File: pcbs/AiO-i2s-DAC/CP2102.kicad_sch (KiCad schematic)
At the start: 12 parts, among them U3 CP2102N

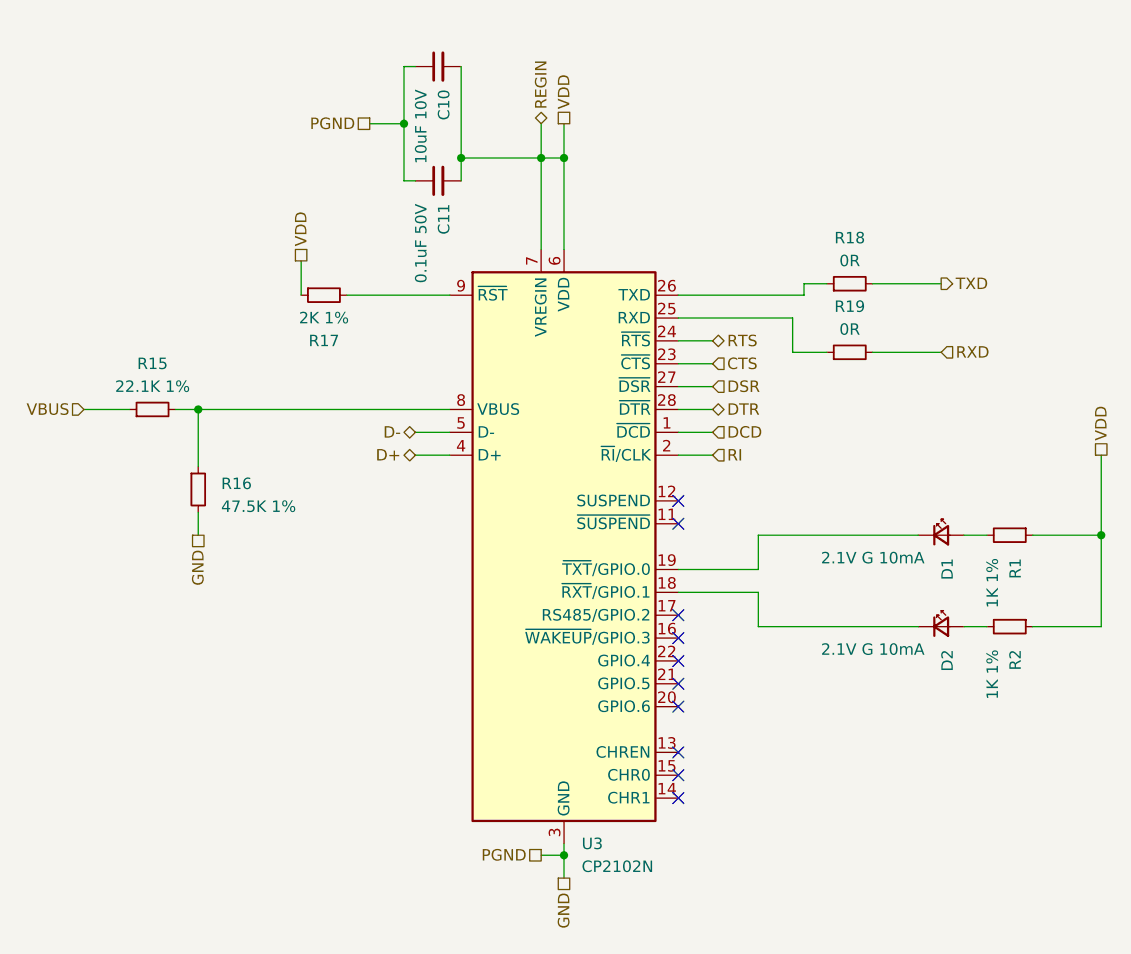
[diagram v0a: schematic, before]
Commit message: Adding equivalent JLCPCB values
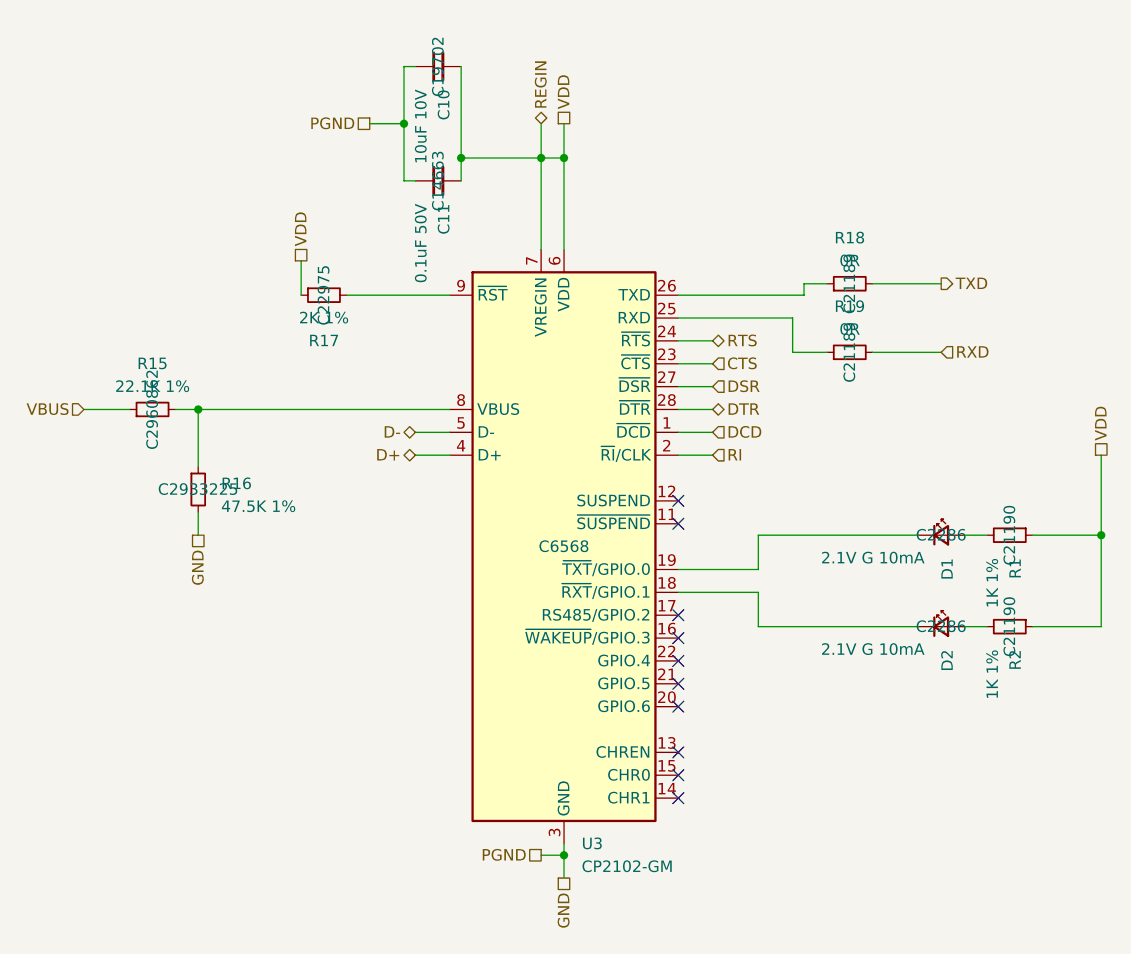
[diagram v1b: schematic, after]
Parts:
- C10: LCSC (none) -> C19702
- C11: LCSC (none) -> C14663
- D1, D2: LCSC (none) -> C2286
- R1, R2: LCSC (none) -> C21190
- R15: LCSC (none) -> C2960862
- R16: LCSC (none) -> C2933225
- R17: LCSC (none) -> C22975
- R18, R19: LCSC (none) -> C21189
- U3: value CP2102N -> CP2102-GM; LCSC (none) -> C6568; Manufacturer_Part_Number CP2102N-A02-GQFN28R -> CP2102-GM
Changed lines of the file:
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@@
+			)
+		)
+		(property "LCSC" "C21190"
+			(at 203.2 100.33 0)
+			(effects
+				(font
+					(size 1.27 1.27)
+				)
 			)
 		)
@@
 			)
 		)
+		(property "LCSC" "C14663"
+			(at 139.7 60.96 0)
+			(effects
+				(font
+					(size 1.27 1.27)
+				)
+			)
+		)
 		(pin "1"
 		)
@@
 			)
 		)
+		(property "LCSC" "C2286"
+			(at 195.58 110.49 0)
+			(effects
+				(font
+					(size 1.27 1.27)
+				)
+			)
+		)
 		(pin "1"
 		)
@@
 				)
 				(hide yes)
+			)
+		)
+		(property "LCSC" "C2286"
+			(at 195.58 100.33 0)
+			(effects
+				(font
+					(size 1.27 1.27)
+				)
 			)
 		)
@@
 			)
 		)
+		(property "LCSC" "C21189"
+			(at 185.42 80.01 0)
+			(effects
+				(font
+					(size 1.27 1.27)
+				)
+			)
+		)
 		(pin "1"
 		)
@@
 			)
 		)
+		(property "LCSC" "C19702"
+			(at 139.7 48.26 0)
+			(effects
+				(font
+					(size 1.27 1.27)
+				)
+			)
+		)
 		(pin "1"
 		)
@@
 			)
 		)
+		(property "LCSC" "C2960862"
+			(at 107.95 86.36 0)
+			(effects
+				(font
+					(size 1.27 1.27)
+				)
+			)
+		)
 		(pin "1"
 		)
@@
 			)
 		)
+		(property "LCSC" "C21190"
+			(at 203.2 110.49 0)
+			(effects
+				(font
+					(size 1.27 1.27)
+				)
+			)
+		)
 		(pin "1"
 		)
@@
 			)
 		)
+		(property "LCSC" "C21189"
+			(at 185.42 72.39 0)
+			(effects
+				(font
+					(size 1.27 1.27)
+				)
+			)
+		)
 		(pin "1"
 		)
@@
 			)
 		)
+		(property "LCSC" "C22975"
+			(at 127 73.66 0)
+			(effects
+				(font
+					(size 1.27 1.27)
+				)
+			)
+		)
 		(pin "1"
 		)
@@
 			)
 		)
+		(property "LCSC" "C2933225"
+			(at 113.03 95.25 0)
+			(effects
+				(font
+					(size 1.27 1.27)
+				)
+			)
+		)
 		(pin "1"
 		)
@@
 			)
 		)
-		(property "Value" "CP2102N"
+		(property "Value" "CP2102-GM"
 			(at 155.6259 137.16 0)
 			(effects
@@
 			)
 		)
-		(property "Datasheet" "https://www.silabs.com/documents/public/data-sheets/cp2102n-datasheet.pdf"
+		(property "Datasheet" "https://www.silabs.com/documents/public/data-sheets/CP2102-9.pdf"
 			(at 154.94 120.65 0)
 			(effects
@@
 			)
 		)
-		(property "Manufacturer_Part_Number" "CP2102N-A02-GQFN28R"
+		(property "Manufacturer_Part_Number" "CP2102-GM"
 			(at 153.67 101.6 0)
 			(effects
@@
 			)
 		)
+		(property "LCSC" "C6568"
+			(at 153.67 101.6 0)
+			(effects
+				(font
+					(size 1.27 1.27)
+				)
+			)
+		)

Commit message: LCSC BOM Preparation
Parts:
- C10: LCSC alt (none) -> C6119842
- C11: LCSC alt (none) -> C1591
- D1, D2: LCSC alt (none) -> C125093
- R1, R2: LCSC alt (none) -> C22548
- R15: LCSC alt (none) -> C2960862
- R16: LCSC alt (none) -> C2933225
- R17: LCSC alt (none) -> C237750
- R18, R19: LCSC alt (none) -> C21189
- U3: LCSC alt (none) -> C6568
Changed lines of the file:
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@@
+			)
+		)
+		(property "LCSC alt" "C22548"
+			(at 203.2 100.33 0)
+			(effects
+				(font
+					(size 1.27 1.27)
+				)
 			)
 		)
@@
 			)
 		)
+		(property "LCSC alt" "C1591"
+			(at 139.7 60.96 0)
+			(effects
+				(font
+					(size 1.27 1.27)
+				)
+			)
+		)
 		(pin "1"
 		)
@@
 			)
 		)
+		(property "LCSC alt" "C125093"
+			(at 195.58 110.49 0)
+			(effects
+				(font
+					(size 1.27 1.27)
+				)
+			)
+		)
 		(pin "1"
 		)
@@
 		)
 		(property "LCSC" "C2286"
+			(at 195.58 100.33 0)
+			(effects
+				(font
+					(size 1.27 1.27)
+				)
+			)
+		)
+		(property "LCSC alt" "C125093"
 			(at 195.58 100.33 0)
 			(effects
@@
 			)
 		)
+		(property "LCSC alt" "C21189"
+			(at 185.42 80.01 0)
+			(effects
+				(font
+					(size 1.27 1.27)
+				)
+			)
+		)
 		(pin "1"
 		)
@@
 			)
 		)
+		(property "LCSC alt" "C6119842"
+			(at 139.7 48.26 0)
+			(effects
+				(font
+					(size 1.27 1.27)
+				)
+			)
+		)
 		(pin "1"
 		)
@@
 			)
 		)
+		(property "LCSC alt" "C2960862"
+			(at 107.95 86.36 0)
+			(effects
+				(font
+					(size 1.27 1.27)
+				)
+			)
+		)
 		(pin "1"
 		)
@@
 			)
 		)
+		(property "LCSC alt" "C22548"
+			(at 203.2 110.49 0)
+			(effects
+				(font
+					(size 1.27 1.27)
+				)
+			)
+		)
 		(pin "1"
 		)
@@
 			)
 		)
+		(property "LCSC alt" "C21189"
+			(at 185.42 72.39 0)
+			(effects
+				(font
+					(size 1.27 1.27)
+				)
+			)
+		)
 		(pin "1"
 		)
@@
 			)
 		)
+		(property "LCSC alt" "C237750"
+			(at 127 73.66 0)
+			(effects
+				(font
+					(size 1.27 1.27)
+				)
+			)
+		)
 		(pin "1"
 		)
@@
 			)
 		)
+		(property "LCSC alt" "C2933225"
+			(at 113.03 95.25 0)
+			(effects
+				(font
+					(size 1.27 1.27)
+				)
+			)
+		)
 		(pin "1"
 		)
@@
 			(at 153.67 101.6 0)
 			(effects
+				(font
+					(size 1.27 1.27)
+				)
+			)
+		)
+		(property "LCSC alt" "C6568"
+			(at 153.67 101.6 0)
+			(effects

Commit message: Build prep
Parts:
- R15: LCSC C2960862 -> C6397988
- R16: LCSC C2933225 -> C403243
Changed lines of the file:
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@@
 					(size 1.27 1.27)
 				)
+				(hide yes)
 			)
 		)
@@
 					(size 1.27 1.27)
 				)
+				(hide yes)
 			)
 		)
@@
 					(size 1.27 1.27)
 				)
+				(hide yes)
 			)
 		)
@@
 					(size 1.27 1.27)
 				)
+				(hide yes)
 			)
 		)
@@
 					(size 1.27 1.27)
 				)
+				(hide yes)
 			)
 		)
@@
 					(size 1.27 1.27)
 				)
+				(hide yes)
 			)
 		)
@@
 					(size 1.27 1.27)
 				)
+				(hide yes)
 			)
 		)
@@
 					(size 1.27 1.27)
 				)
+				(hide yes)
 			)
 		)
@@
 					(size 1.27 1.27)
 				)
+				(hide yes)
 			)
 		)
@@
 					(size 1.27 1.27)
 				)
+				(hide yes)
 			)
 		)
@@
 					(size 1.27 1.27)
 				)
+				(hide yes)
 			)
 		)
@@
 					(size 1.27 1.27)
 				)
+				(hide yes)
 			)
 		)
@@
 			)
 		)
-		(property "LCSC" "C2960862"
+		(property "LCSC" "C6397988"
 			(at 107.95 86.36 0)
 			(effects
@@
 					(size 1.27 1.27)
 				)
+				(hide yes)
 			)
 		)
@@
 					(size 1.27 1.27)
 				)
+				(hide yes)
 			)
 		)
@@
 					(size 1.27 1.27)
 				)
+				(hide yes)
 			)
 		)
@@
 					(size 1.27 1.27)
 				)
+				(hide yes)
 			)
 		)
@@
 					(size 1.27 1.27)
 				)
+				(hide yes)
 			)
 		)
@@
 					(size 1.27 1.27)
 				)
+				(hide yes)
 			)
 		)
@@
 					(size 1.27 1.27)
 				)
+				(hide yes)
 			)
 		)
@@
 					(size 1.27 1.27)
 				)
+				(hide yes)
 			)
 		)
@@
 			)
 		)
-		(property "LCSC" "C2933225"
+		(property "LCSC" "C403243"
 			(at 113.03 95.25 0)
 			(effects
@@
 					(size 1.27 1.27)
 				)
+				(hide yes)
 			)
 		)
@@
 					(size 1.27 1.27)
 				)
-			)
-		)
+				(hide yes)
+			)
+		)

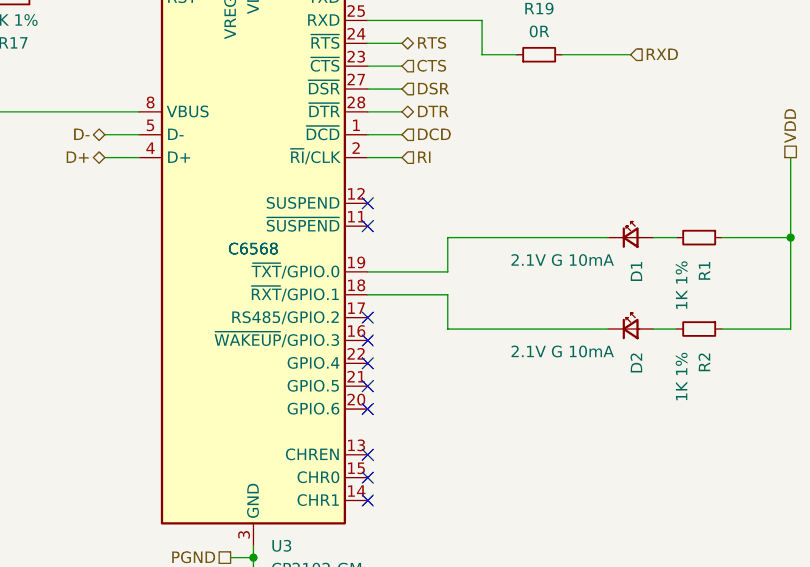
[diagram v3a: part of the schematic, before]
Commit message: UART0 LEDs correction
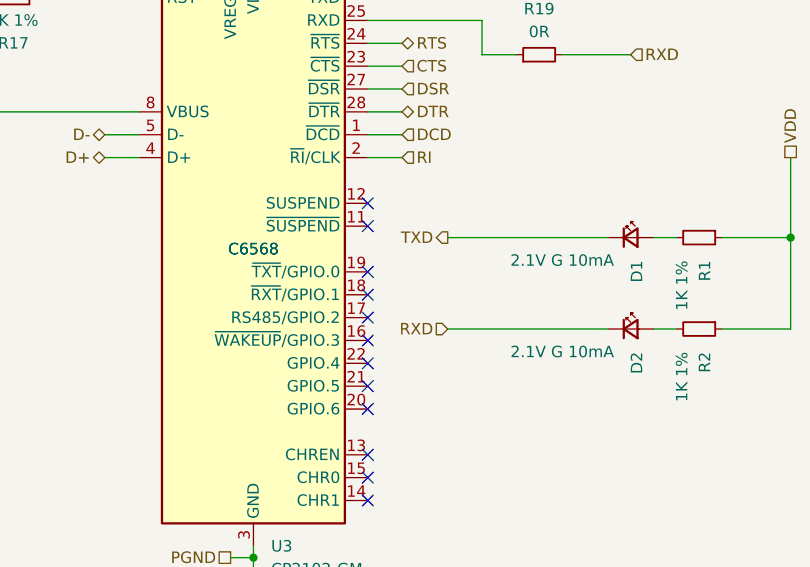
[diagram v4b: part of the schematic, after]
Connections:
- net RXD: now also D2.1 (K)
- net TXD: now also D1.1 (K)
- net at U3.18 (~{RXT}/GPIO.1): no longer D2.1 (K)
- net at U3.19 (~{TXT}/GPIO.0): no longer D1.1 (K)
- no-connect marks 10 -> 12
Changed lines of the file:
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@@
 	(title_block
 		(title "AiO-i2s-DAC")
-		(date "2025-06-04")
-		(rev "0.1.5")
+		(date "2025-10-05")
+		(rev "0.1.7")
 		(company "Martin Roger")
 	)
@@
 	)
 	(no_connect
+		(at 166.37 104.14)
+	)
+	(no_connect
 		(at 166.37 116.84)
 	)
@@
 	)
 	(no_connect
+		(at 166.37 106.68)
+	)
+	(no_connect
 		(at 166.37 99.06)
 	)
@@
 	(wire
 		(pts
-			(xy 175.26 104.14) (xy 166.37 104.14)
-		)
-		(stroke
-			(width 0)
-			(type default)
-		)
-	)
-	(wire
-		(pts
 			(xy 137.16 88.9) (xy 140.97 88.9)
 		)
@@
 	(wire
 		(pts
-			(xy 175.26 110.49) (xy 175.26 106.68)
-		)
-		(stroke
-			(width 0)
-			(type default)
-		)
-	)
-	(wire
-		(pts
-			(xy 175.26 100.33) (xy 175.26 104.14)
-		)
-		(stroke
-			(width 0)
-			(type default)
-		)
-	)
-	(wire
-		(pts
 			(xy 187.96 80.01) (xy 195.58 80.01)
 		)
@@
 		(pts
 			(xy 113.03 86.36) (xy 113.03 92.71)
-		)
-		(stroke
-			(width 0)
-			(type default)
-		)
-	)
-	(wire
-		(pts
-			(xy 175.26 106.68) (xy 166.37 106.68)
 		)
 		(stroke
@@
 		)
 	)
+	(hierarchical_label "RXD"
+		(shape input)
+		(at 175.26 110.49 180)
+		(effects
+			(font
+				(size 1.27 1.27)
+			)
+			(justify right)
+		)
+	)
 	(hierarchical_label "CTS"
 		(shape input)
@@
 		)
 	)
+	(hierarchical_label "TXD"
+		(shape output)
+		(at 175.26 100.33 180)
+		(effects
+			(font
+				(size 1.27 1.27)
+			)
+			(justify right)
+		)
+	)
